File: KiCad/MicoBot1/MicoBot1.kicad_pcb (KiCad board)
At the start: 2 copper layers, 50 x 50 mm, 14 parts, among them J1 Conn_01x06_Male, J2 Screw_Terminal_01x02, J3 Conn_01x06_Male, SW1 SW_Push, SW2 SW_SPDT, U1 ATmega328P-PU, U2 L293D, U3 AMS1117-5.0, Y1 Crystal_Small

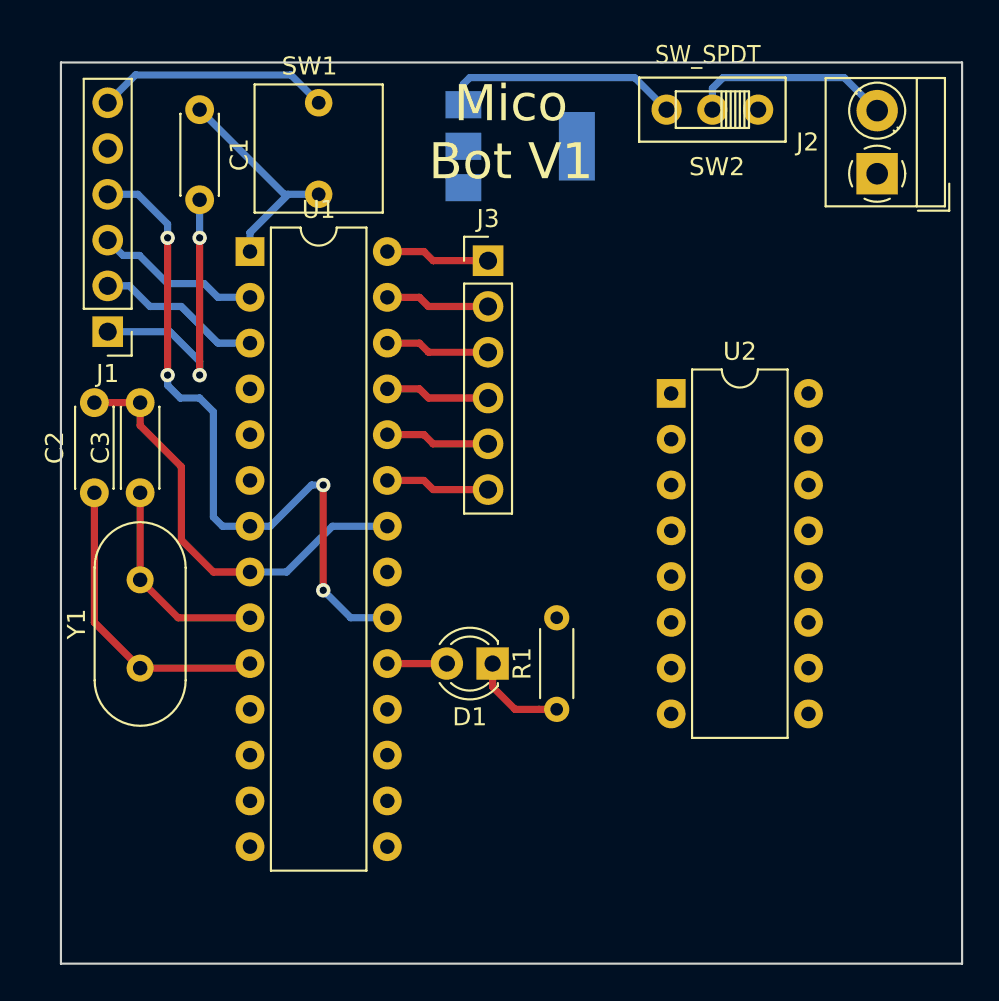
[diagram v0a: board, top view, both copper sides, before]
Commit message: 
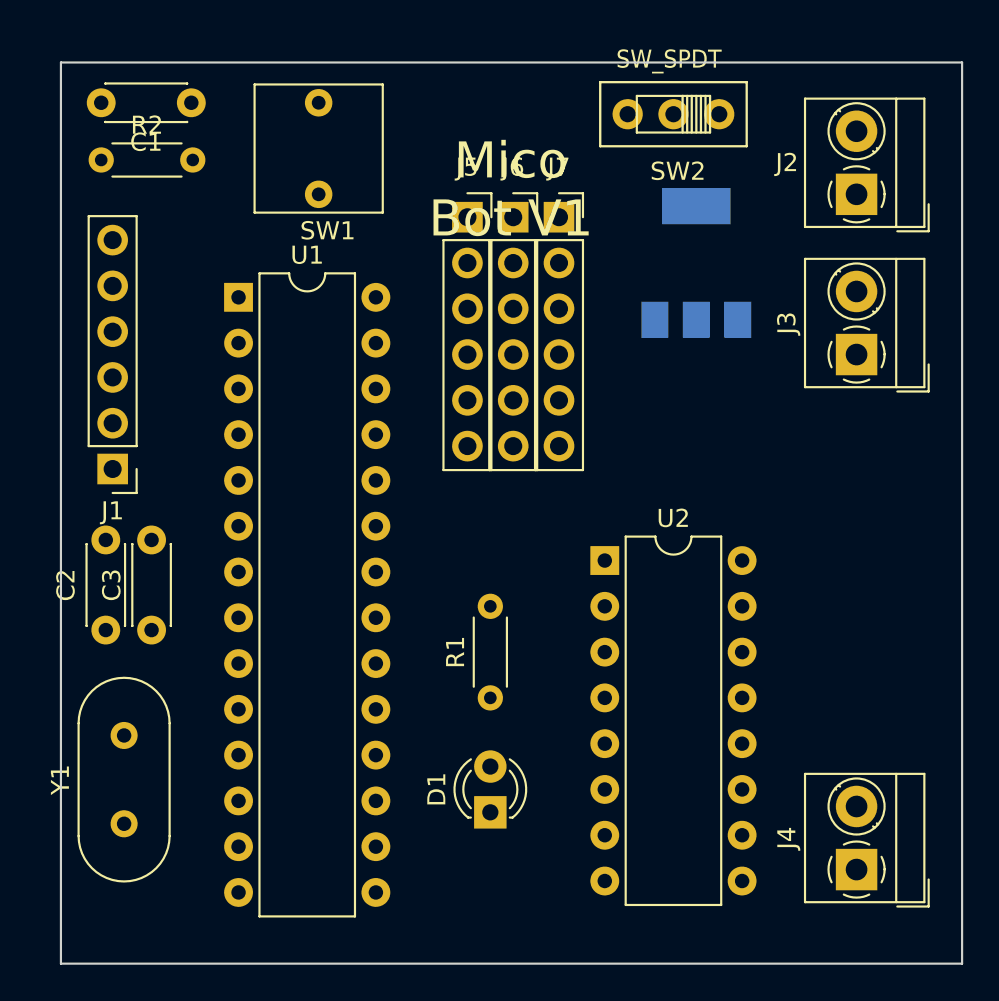
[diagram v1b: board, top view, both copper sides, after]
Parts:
- added J4: Screw_Terminal_01x02, TerminalBlock_MetzConnect:TerminalBlock_MetzConnect_Type059_RT06302HBWC_1x02_P3.50mm_Horizontal, F.Cu at (144.1, 144.8)
- added J5: Conn_01x06_Male, Connector_PinSocket_2.54mm:PinSocket_1x06_P2.54mm_Vertical, F.Cu at (122.6, 108.6)
- added J6: Conn_01x06_Male, Connector_PinSocket_2.54mm:PinSocket_1x06_P2.54mm_Vertical, F.Cu at (125.1, 108.6)
- added J7: Conn_01x06_Male, Connector_PinSocket_2.54mm:PinSocket_1x06_P2.54mm_Vertical, F.Cu at (127.6, 108.6)
- added R2: R, Resistor_THT:R_Axial_DIN0204_L3.6mm_D1.6mm_P5.08mm_Horizontal, F.Cu at (102.2, 105.4)
- J3: value Conn_01x06_Male -> Screw_Terminal_01x02; footprint Connector_PinHeader_2.54mm:PinHeader_1x06_P2.54mm_Vertical -> TerminalBlock_MetzConnect:TerminalBlock_MetzConnect_Type059_RT06302HBWC_1x02_P3.50mm_Horizontal
- moved J3 21.1 mm to (144.1, 116.2), turned to 90 degrees
- moved U3 11.7 mm to (135.3, 111.1), turned to 90 degrees
- moved U2 9.98 mm to (130.2, 127.6)
- moved Y1 8.68 mm to (103.5, 142.2)
- moved D1 8.26 mm to (123.8, 141.6), turned to 90 degrees
- moved C2 7.65 mm to (102.5, 131.5)
- moved C3 7.65 mm to (105.0, 131.5)
- moved J1 7.62 mm to (102.9, 122.6)
- moved SW1 5.08 mm to (116.8, 104.8), turned to 270 degrees
- moved R1 3.74 mm to (123.8, 135.3)
- moved U1 2.62 mm to (109.9, 113.0)
- moved SW2 2.17 mm to (134.0, 102.9)
- moved J2 1.62 mm to (144.1, 107.3)
- moved C1 0.60 mm to (107.2, 102.2), turned to 180 degrees
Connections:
- SW2 pad 3: Net-(SW2-Pad3) -> VSS
- U1 pad 23: Net-(J3-Pad6) -> Net-(J5-Pad6)
- U1 pad 24: Net-(J3-Pad5) -> Net-(J5-Pad5)
- U1 pad 25: Net-(J3-Pad4) -> Net-(J5-Pad4)
- U1 pad 26: Net-(J3-Pad3) -> Net-(J5-Pad3)
- U1 pad 27: Net-(J3-Pad2) -> Net-(J5-Pad2)
- U1 pad 28: Net-(J3-Pad1) -> Net-(J5-Pad1)
- U2 pad 1: Net-(U2-Pad1) -> Net-(U1-Pad15)
- U2 pad 10: Net-(U2-Pad10) -> Net-(U1-Pad18)
- U2 pad 15: Net-(U2-Pad15) -> Net-(U1-Pad17)
- U2 pad 16: Net-(U2-Pad16) -> VCC
- U2 pad 2: Net-(U2-Pad2) -> Net-(U1-Pad13)
- U2 pad 3: Net-(U2-Pad3) -> Net-(J3-Pad1)
- U2 pad 6: Net-(U2-Pad6) -> Net-(J3-Pad2)
- U2 pad 7: Net-(U2-Pad7) -> Net-(U1-Pad14)
- U2 pad 8: Net-(U2-Pad8) -> VSS
- U2 pad 9: Net-(U2-Pad9) -> Net-(U1-Pad16)
- U3 pad 3: Net-(SW2-Pad3) -> VSS
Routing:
- net VCC: track 39.2 -> 0.00 mm, vias 4 -> 0
- net GND: track 37.3 -> 0.00 mm
- net Net-(C2-Pad1): track 17.0 -> 0.00 mm
- net Net-(C1-Pad2): track 16.3 -> 0.00 mm, vias 2 -> 0
- net Net-(SW2-Pad3): track 13.3 -> 0.00 mm
- net Net-(C1-Pad1): track 12.7 -> 0.00 mm
- net Net-(C3-Pad1): track 11.8 -> 0.00 mm
- net Net-(J2-Pad2): track 11.3 -> 0.00 mm
- net Net-(J1-Pad3): track 9.21 -> 0.00 mm
- net Net-(J1-Pad2): track 9.21 -> 0.00 mm
- net Net-(J3-Pad3): track 5.80 -> 0.00 mm
- net Net-(J3-Pad1): track 5.80 -> 0.00 mm
- net Net-(J3-Pad4): track 5.80 -> 0.00 mm
- net Net-(J3-Pad2): track 5.80 -> 0.00 mm
- net Net-(J3-Pad6): track 5.80 -> 0.00 mm
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
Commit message: 
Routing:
- net Net-(J2-Pad2): track 0.00 -> 13.0 mm
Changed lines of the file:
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@@
     (thickness 1.6)
     (drawings 6)
-    (tracks 0)
+    (tracks 5)
     (zones 0)
     (modules 19)
@@
   )
   (setup
-    (last_trace_width 0.25)
+    (last_trace_width 0.4)
     (user_trace_width 0.4)
     (user_trace_width 0.5)
@@
   (gr_line (start 150 150) (end 150 100) (layer Edge.Cuts) (width 0.12))
   (gr_line (start 100 150) (end 150 150) (layer Edge.Cuts) (width 0.12))
+  (segment (start 142.518655 103.815) (end 140.923655 105.41) (width 0.4) (layer B.Cu) (net 7))
+  (segment (start 144.145 103.815) (end 142.518655 103.815) (width 0.4) (layer B.Cu) (net 7))
+  (segment (start 140.923655 105.41) (end 134.62 105.41) (width 0.4) (layer B.Cu) (net 7))
+  (segment (start 133.985 104.775) (end 133.985 102.87) (width 0.4) (layer B.Cu) (net 7))
+  (segment (start 134.62 105.41) (end 133.985 104.775) (width 0.4) (layer B.Cu) (net 7))
 )

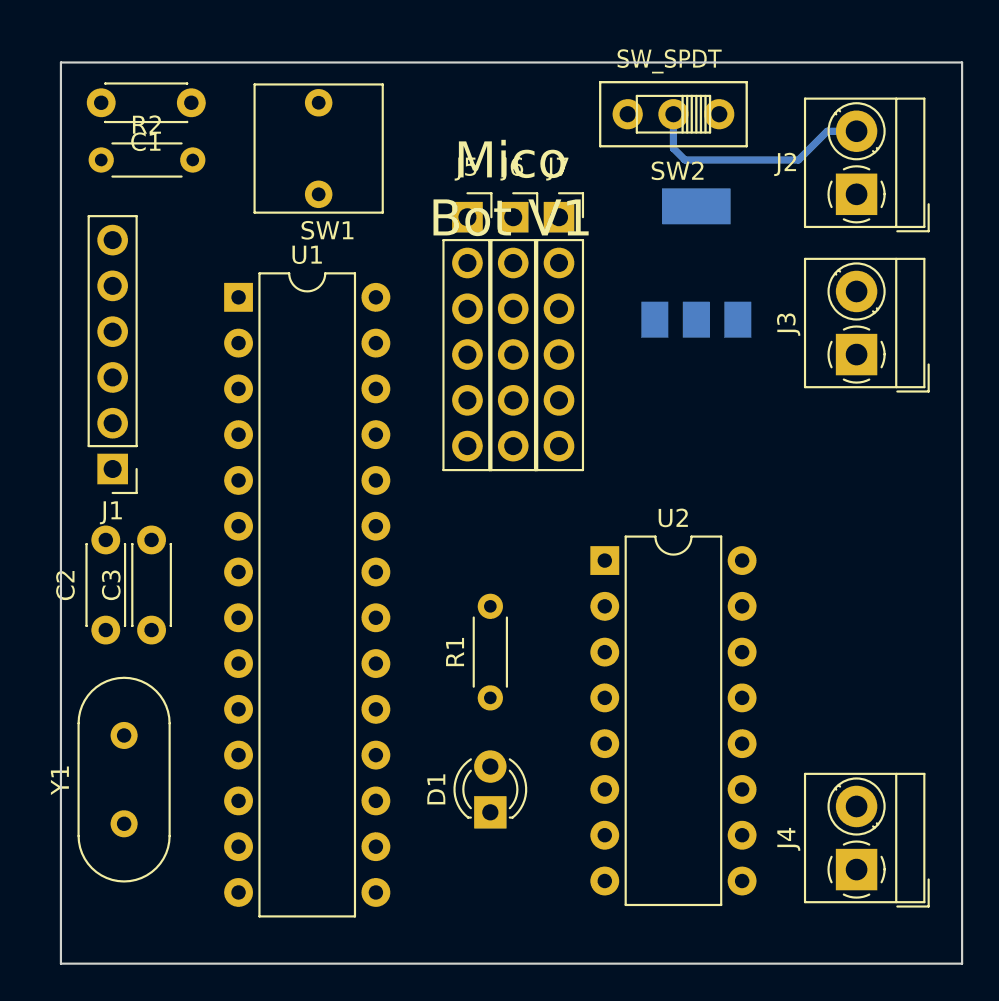
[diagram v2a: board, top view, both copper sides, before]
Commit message: 
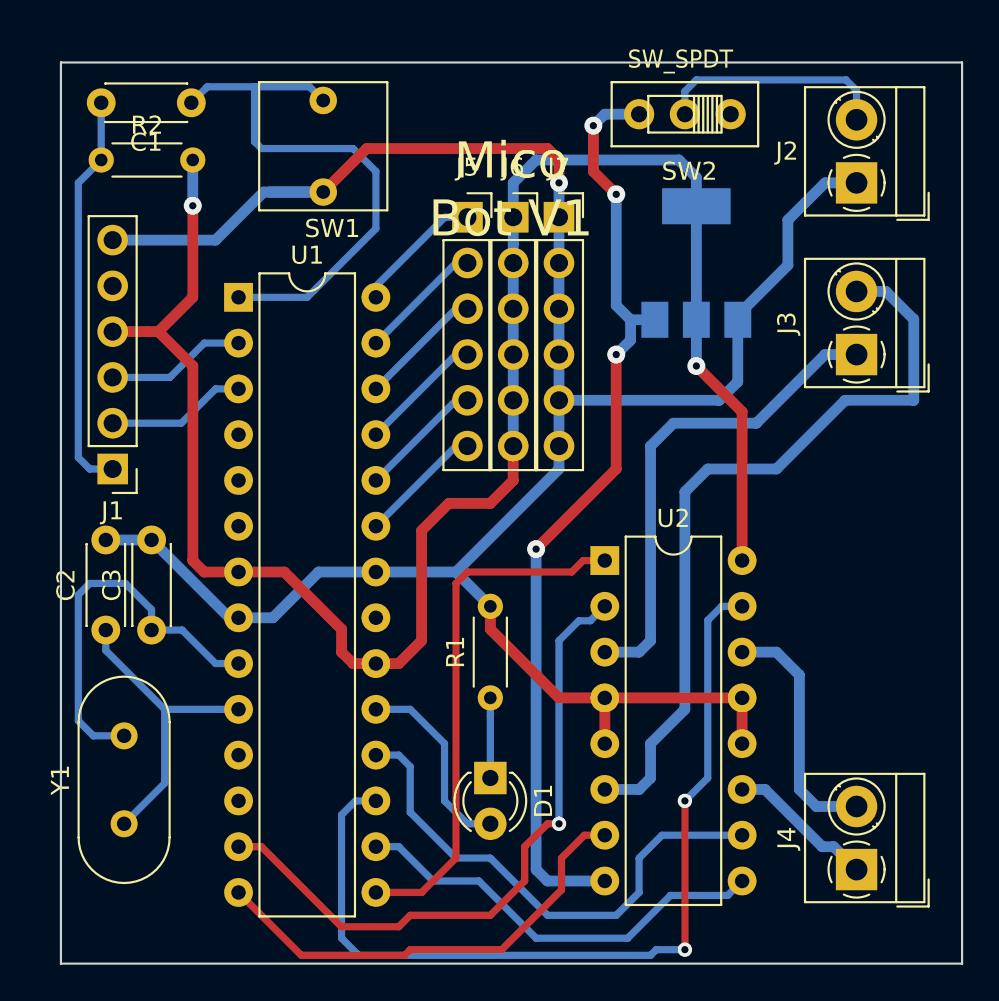
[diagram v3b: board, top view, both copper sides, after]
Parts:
- Y1: footprint Crystal:Crystal_HC18-U_Vertical -> Crystal:Crystal_HC49-4H_Vertical
- moved D1 1.91 mm to (123.8, 139.7), turned to 270 degrees
- moved J2 0.63 mm to (144.1, 106.7)
- moved SW2 0.63 mm to (134.6, 102.9)
- moved SW1 0.28 mm to (117.1, 104.6)
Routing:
- net GND: track 0.00 -> 127.4 mm, vias 0 -> 1
- net VCC: track 0.00 -> 104.4 mm, vias 0 -> 2
- net VSS: track 0.00 -> 52.8 mm, vias 0 -> 4
- net Net-(U1-Pad17): track 0.00 -> 49.7 mm, vias 0 -> 2
- net Net-(J3-Pad2): track 0.00 -> 42.6 mm
- net Net-(U1-Pad13): track 0.00 -> 36.6 mm, vias 0 -> 1
- net Net-(C1-Pad1): track 0.00 -> 30.8 mm
- net Net-(U1-Pad15): track 0.00 -> 29.3 mm
- net Net-(U1-Pad18): track 0.00 -> 28.4 mm
- net Net-(J3-Pad1): track 0.00 -> 27.1 mm
- net Net-(U1-Pad14): track 0.00 -> 25.6 mm
- net Net-(U1-Pad16): track 0.00 -> 23.7 mm
- net Net-(C1-Pad2): track 0.00 -> 22.4 mm
- net Net-(C3-Pad1): track 0.00 -> 21.5 mm
- net Net-(C2-Pad1): track 0.00 -> 17.1 mm
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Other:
- net class Default: trace_width 0.25 -> 0.4
- net class MicoBot added: clearance 0.3, trace_width 0.6, via_dia 1, via_drill 0.4
